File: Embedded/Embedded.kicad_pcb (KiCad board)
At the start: 2 copper layers, 77.5 x 103 mm, 121 parts, among them J1 GyroBreakout, J10 TouchButton, J11 USB-C Breakout, J2 BaseResMUX, J3 BaseNeoMUX, J4 HelixNeo, J5 FanConnector, J6 Conn_01x08, J7 Conn_01x08, J8 Speaker, J9 LightSensor, Q1 FQP27P06, Q2 FS8205A, Q3 AO3401A, Q4 FS8205A, Q5 AO3401A, Q6 FS8205A, Q7 AO3401A, Q8 FS8205A, Q9 AO3401A, SW1 BackboardSw, SW2 BackboardSw, U1 ESP32-C6-WROOM-1, U10 DW01A, U2 BQ25895RTW, U3 FSUSB30MUX, U4 DW01A, U5 MP8715, U6 DW01A, U7 SN74AHCT125N, U8 SN74AHCT125N, U9 DW01A

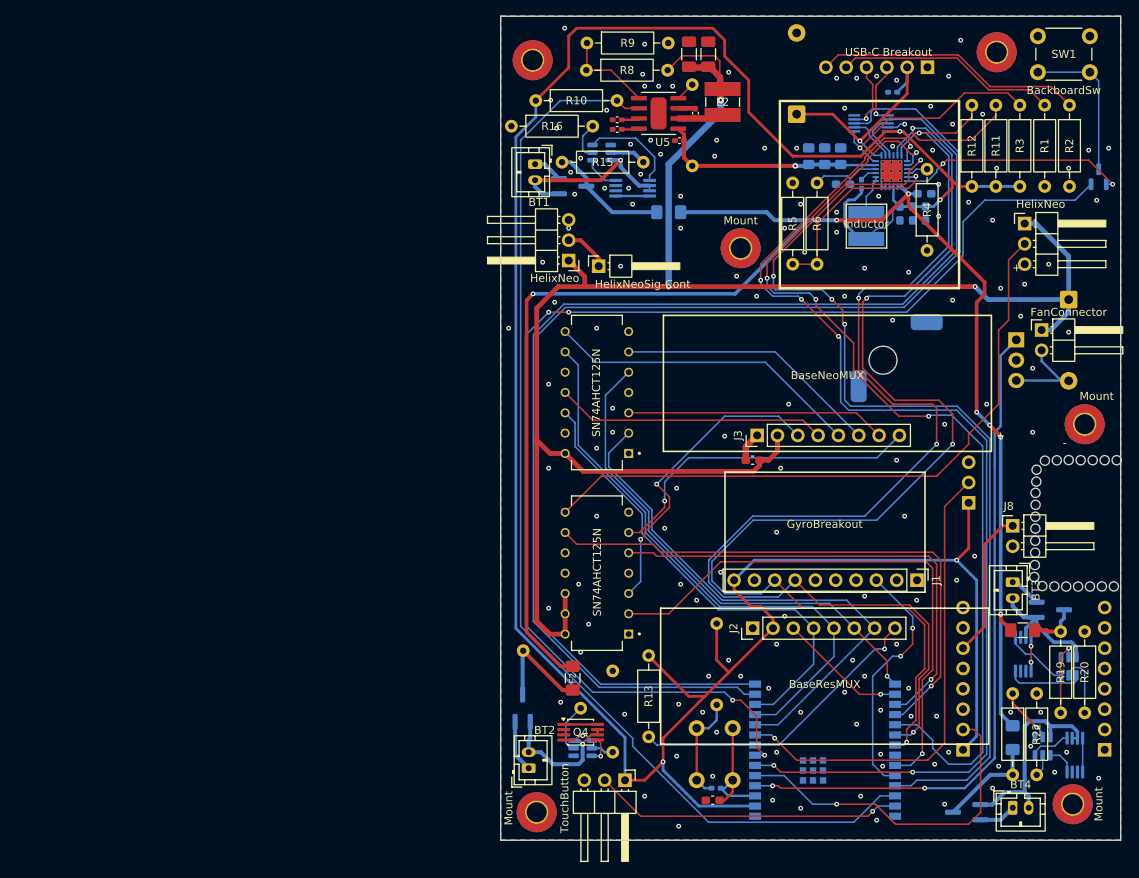
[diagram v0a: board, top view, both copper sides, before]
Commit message: Overhaul
Redesign, Ground for UWP/Droid app, Switch from Arduino C to ESP-IDF with native C
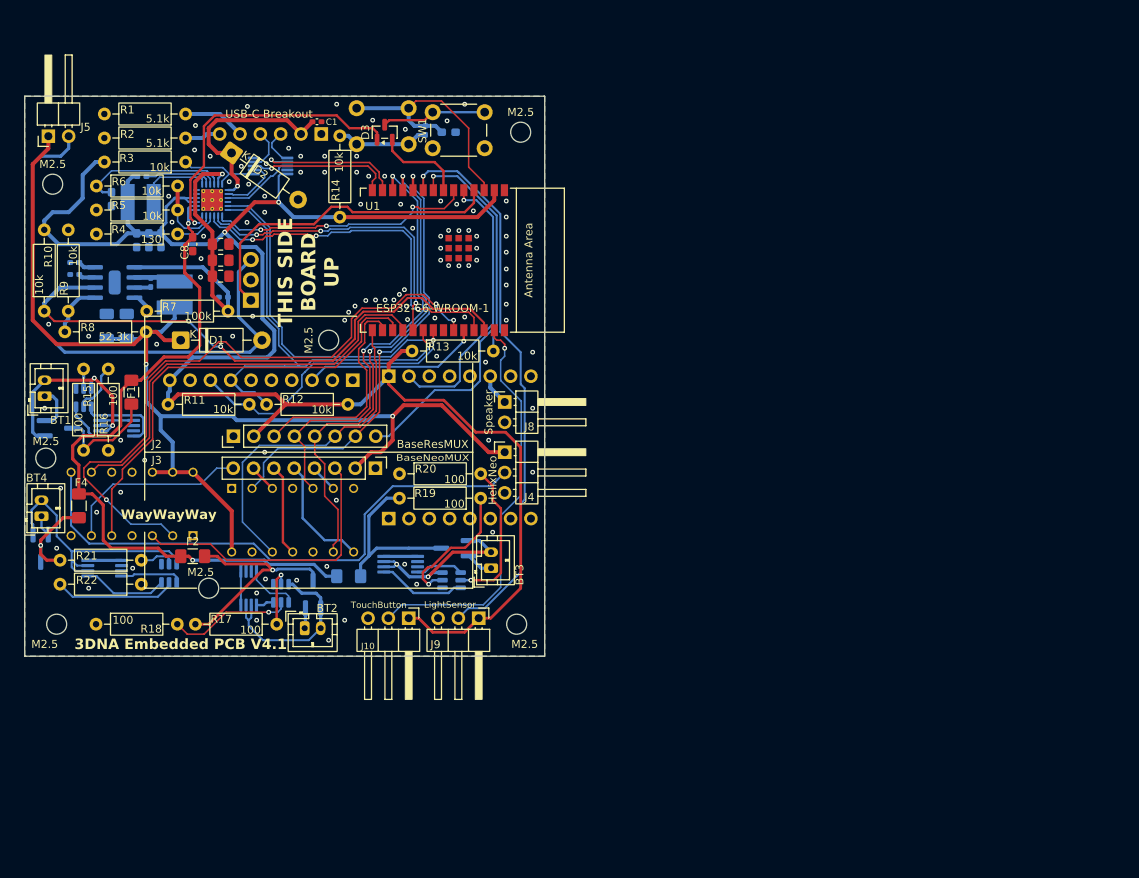
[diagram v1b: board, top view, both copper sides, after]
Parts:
- removed ? (x25): , 
- removed the C17 at (141.0, 95.5)
- removed the C17 at (136.4, 136.5)
- removed HelixNeoSig-Cont: PinHeader_1x01_P2.54mm_Horizontal, Connector_PinHeader_2.54mm:PinHeader_1x01_P2.54mm_Horizontal
- removed the J4 at (118.0, 70.5)
- removed the J4 at (175.0, 65.9)
- removed Mount (x6): MountingHole_2.5mm_Pad_TopBottom, MountingHole:MountingHole_2.5mm_Pad_TopBottom
- removed the REF** at (186.1, 111.3)
- removed the REF** at (129.2, 52.2)
- added C17: 100nF, Capacitor_SMD:C_0402_1005Metric_Pad0.74x0.62mm_HandSolder, B.Cu at (100.1, 54.3)
- added J4: HelixNeo, Connector_PinHeader_2.54mm:PinHeader_1x03_P2.54mm_Horizontal, F.Cu at (110.0, 94.5)
- added M2.5: MountingHole_2.5mm, MountingHole:MountingHole_2.5mm, F.Cu at (73.0, 111.5)
- added M2.5: MountingHole_2.5mm, MountingHole:MountingHole_2.5mm, F.Cu at (112.0, 54.5)
- added M2.5: MountingHole_2.5mm, MountingHole:MountingHole_2.5mm, F.Cu at (54.0, 116.0)
- added M2.5: MountingHole_2.5mm, MountingHole:MountingHole_2.5mm, F.Cu at (52.6, 95.2)
- added M2.5: MountingHole_2.5mm, MountingHole:MountingHole_2.5mm, F.Cu at (53.5, 61.0)
- added M2.5: MountingHole_2.5mm, MountingHole:MountingHole_2.5mm, F.Cu at (111.5, 116.0)
- added M2.5: MountingHole_2.5mm, MountingHole:MountingHole_2.5mm, F.Cu at (88.0, 80.5)
- added REF**: SolderWirePad_1x01_SMD_1.5x3mm, Connector_Wire:SolderWirePad_1x01_SMD_1.5x3mm, B.Cu at (61.3, 73.3)
- C1, C2, C3, C4, C8, D1, D2, D3, F1, F4, J9, R14, R17, R18, R7, U1: moved to F.Cu
- C11, C12, C13, C14, C15, C16, C18, F3, J1, L2, Q4, U5, U7, U8: moved to B.Cu
- moved BT4 126.8 mm to (52.1, 102.5), turned to 90 degrees
- moved J5 126.5 mm to (53.0, 55.0), turned to 90 degrees
- moved Q8 123.5 mm to (60.0, 109.0), turned to 180 degrees
- moved Q9 120.4 mm to (52.0, 106.5), turned to -90 degrees
- moved F4 120.3 mm to (56.8, 101.2)
- moved R22 112.8 mm to (64.6, 111.0), turned to 180 degrees
- moved U10 111.3 mm to (68.0, 109.6)
- moved D1 111.1 mm to (69.5, 80.5), turned to 0 degrees
- moved R2 110.6 mm to (70.1, 55.2), turned to 180 degrees
- moved R21 110.2 mm to (64.6, 108.0), turned to 180 degrees
- moved R1 107.4 mm to (70.1, 52.2), turned to 180 degrees
- moved R11 107.0 mm to (67.9, 88.5), turned to 0 degrees
- moved R3 104.5 mm to (70.1, 58.2), turned to 180 degrees
- moved R4 103.9 mm to (59.0, 67.2), turned to 0 degrees
- moved Q1 95.8 mm to (78.3, 75.5), turned to 90 degrees
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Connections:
- U7 pad 11: /BaseNeoS0 -> /BaseNeoS2
- U7 pad 12: /MuxS0 -> /MuxS2
- U7 pad 5: /MuxS2 -> /MuxS0
- U7 pad 6: /BaseNeoS2 -> /BaseNeoS0
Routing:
- net /BackboardBtn: track 157.3 -> 11.2 mm, vias 4 -> 0
- net /EspD+: track 152.5 -> 18.2 mm, vias 0 -> 1
- net /EspD-: track 147.0 -> 18.8 mm, vias 0 -> 1
- net /BmsInt: track 141.0 -> 33.2 mm, vias 6 -> 3
- net BATT: track 196.8 -> 90.8 mm, vias 7 -> 2
- net +3.3V: track 334.3 -> 231.5 mm, vias 4 -> 2
- net /SDA: track 153.9 -> 59.4 mm, vias 4 -> 1
- net /SCL: track 161.9 -> 78.1 mm, vias 4 -> 1
- net /BmsOTG: track 121.5 -> 38.6 mm, vias 4 -> 3
- net /BmsCE: track 124.2 -> 45.7 mm, vias 4 -> 3
- net +5V: track 217.8 -> 147.1 mm, vias 3 -> 2
- net /BuckPOK: track 136.9 -> 72.5 mm, vias 0 -> 2
- net /FanOut: track 12.3 -> 69.2 mm
- net /FanControl: track 85.0 -> 41.2 mm, vias 2 -> 0
- net /BaseNeoS0: track 33.8 -> 3.50 mm
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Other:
- board size 77.5 x 103 mm -> 65 x 70 mm
- board text added: "3DNA Embedded PCB V4.1"
- board text added: "THIS SIDE BOARD UP"
- board text added: "WayWayWay"
- board text removed: "+"
- board text removed: "-"
- board text removed: "Inductor"
- board text removed: "SIG"
- board text removed: "VCC"

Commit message: PCB changes + new readme
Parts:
- J5: footprint Connector_PinHeader_2.54mm:PinHeader_1x02_P2.54mm_Horizontal -> Connector_JST:JST_XH_B2B-XH-A_1x02_P2.50mm_Vertical
- L2: value 3.3~4.7uH -> 4.7uH
- moved M2.5 7.57 mm to (54.5, 53.5)
- moved J5 7.02 mm to (53.5, 62.0)
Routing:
- net /FanOut: track 69.2 -> 63.3 mm
- net +5V: track 147.1 -> 141.2 mm
- net /DFPlayer: track 35.2 -> 36.4 mm
- net +3.3V: track 231.5 -> 232.5 mm
- net GND: vias 101 -> 131
